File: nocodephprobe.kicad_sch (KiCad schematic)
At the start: 30 parts, among them J1 RF1-01 BNC, J2 10K, Q1 2N7002, U1 LMV358a, U2 ICL7106CPL, U3 MCP1501T-10E/CHY, U4 VI-302-DP-RC-S

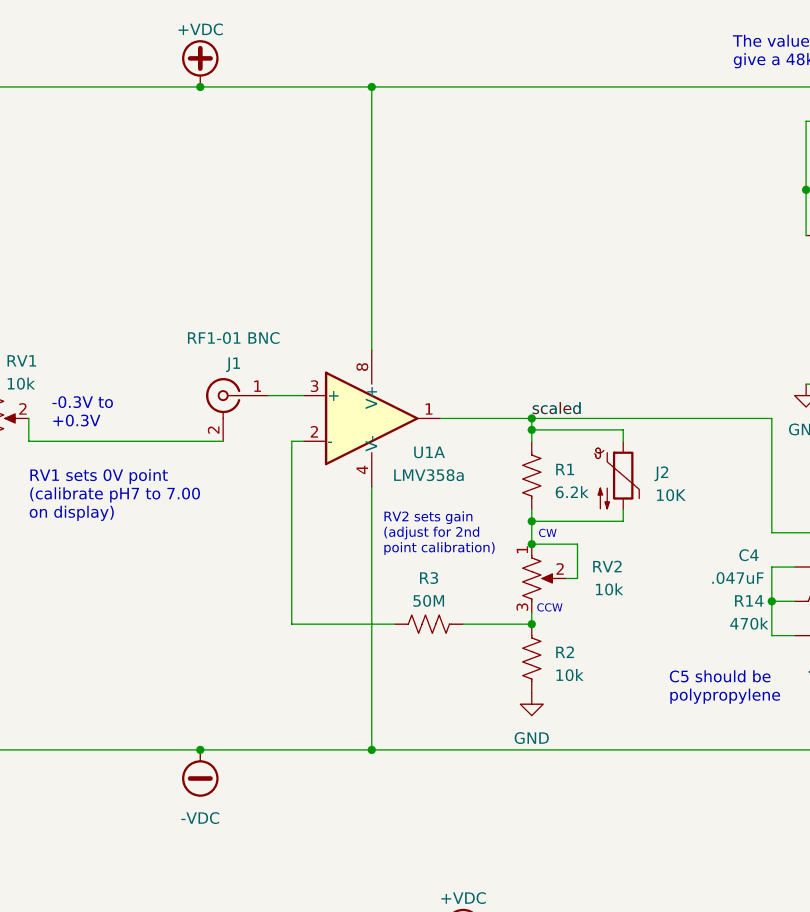
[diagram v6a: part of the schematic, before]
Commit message: schematic: add decoupling caps to op-amp
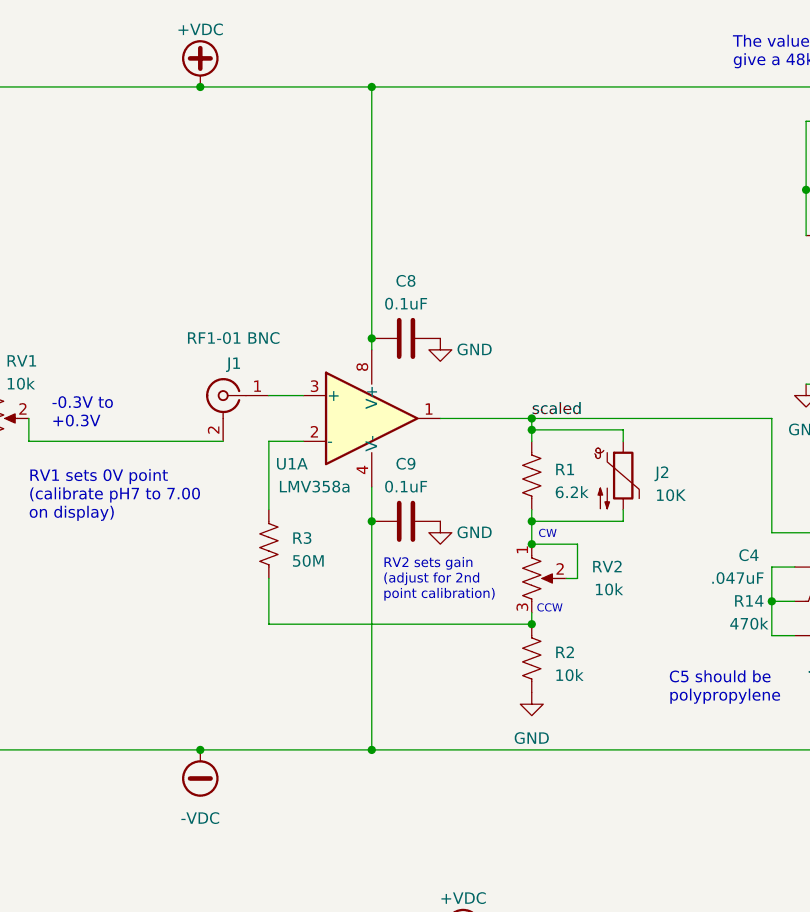
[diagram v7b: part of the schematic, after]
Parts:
- added C8, C9: 0.1uF, Capacitor_SMD:C_0805_2012Metric_Pad1.18x1.45mm_HandSolder, symbol Device:C
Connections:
- net +VDC: now also C8.1
- net -VDC: now also C9.1
- net GND: now also C8.2, C9.2
- net at U1.2 (-): now also R3.1; no longer R3.2
- net at R2.2, RV2.3: now also R3.2; no longer R3.1
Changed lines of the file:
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@@
   (junction (at 68.58 142.24) (diameter 0) (color 0 0 0 0)
   )
+  (junction (at 124.46 54.61) (diameter 0) (color 0 0 0 0)
+  )
   (junction (at 275.59 90.17) (diameter 0) (color 0 0 0 0)
   )
@@
   )
   (junction (at 71.12 74.93) (diameter 0) (color 0 0 0 0)
+  )
+  (junction (at 124.46 74.93) (diameter 0) (color 0 0 0 0)
   )
   (junction (at 275.59 85.09) (diameter 0) (color 0 0 0 0)
@@
     (stroke (width 0) (type default))
   )
+  (wire (pts (xy 113.03 86.36) (xy 142.24 86.36))
+    (stroke (width 0) (type default))
+  )
   (wire (pts (xy 74.93 53.34) (xy 74.93 59.69))
     (stroke (width 0) (type default))
@@
     (stroke (width 0) (type default))
   )
-  (wire (pts (xy 115.57 86.36) (xy 127 86.36))
-    (stroke (width 0) (type default))
-  )
   (wire (pts (xy 82.55 53.34) (xy 74.93 53.34))
     (stroke (width 0) (type default))
@@
     (stroke (width 0) (type default))
   )
+  (wire (pts (xy 124.46 54.61) (xy 124.46 55.88))
+    (stroke (width 0) (type default))
+  )
   (wire (pts (xy 232.41 67.31) (xy 240.03 67.31))
     (stroke (width 0) (type default))
@@
     (stroke (width 0) (type default))
   )
-  (wire (pts (xy 134.62 86.36) (xy 142.24 86.36))
-    (stroke (width 0) (type default))
-  )
   (wire (pts (xy 152.4 64.77) (xy 152.4 66.04))
     (stroke (width 0) (type default))
@@
     (stroke (width 0) (type default))
   )
+  (wire (pts (xy 113.03 73.66) (xy 113.03 66.04))
+    (stroke (width 0) (type default))
+  )
   (wire (pts (xy 232.41 50.8) (xy 217.17 50.8))
     (stroke (width 0) (type default))
@@
     (stroke (width 0) (type default))
   )
-  (wire (pts (xy 124.46 71.12) (xy 124.46 100.33))
-    (stroke (width 0) (type default))
-  )
   (wire (pts (xy 217.17 76.2) (xy 227.33 76.2))
     (stroke (width 0) (type default))
@@
     (stroke (width 0) (type default))
   )
-  (wire (pts (xy 124.46 26.67) (xy 124.46 55.88))
+  (wire (pts (xy 124.46 26.67) (xy 124.46 54.61))
     (stroke (width 0) (type default))
   )
@@
     (stroke (width 0) (type default))
   )
-  (wire (pts (xy 115.57 86.36) (xy 115.57 66.04))
+  (wire (pts (xy 113.03 86.36) (xy 113.03 81.28))
     (stroke (width 0) (type default))
   )
@@
     (stroke (width 0) (type default))
   )
-  (wire (pts (xy 115.57 66.04) (xy 116.84 66.04))
+  (wire (pts (xy 113.03 66.04) (xy 116.84 66.04))
     (stroke (width 0) (type default))
   )
@@
     (stroke (width 0) (type default))
   )
+  (wire (pts (xy 124.46 71.12) (xy 124.46 74.93))
+    (stroke (width 0) (type default))
+  )
   (wire (pts (xy 186.69 86.36) (xy 186.69 87.63))
     (stroke (width 0) (type default))
@@
   )
   (wire (pts (xy 168.91 80.01) (xy 171.45 80.01))
+    (stroke (width 0) (type default))
+  )
+  (wire (pts (xy 124.46 74.93) (xy 124.46 100.33))
     (stroke (width 0) (type default))
   )
@@
     (effects (font (size 1.27 1.27)) (justify left bottom))
   )
-  (text "RV2 sets gain\n(adjust for 2nd\npoint calibration)" (at 125.73 78.74 0)
+  (text "RV2 sets gain\n(adjust for 2nd\npoint calibration)" (at 125.73 83.82 0)
     (effects (font (size 1.0668 1.0668)) (justify left bottom))
   )
@@
     )
   )
+  (symbol (lib_id "Device:R_US") (at 113.03 77.47 0) (unit 1)
+    (in_bom yes) (on_board yes) (dnp no) (fields_autoplaced)
+    (property "Reference" "R3" (at 115.57 76.835 0)
+      (effects (font (size 1.27 1.27)) (justify left))
+    )
+    (property "Value" "50M" (at 115.57 79.375 0)
+      (effects (font (size 1.27 1.27)) (justify left))
+    )
+    (property "Footprint" "Resistor_SMD:R_0805_2012Metric_Pad1.20x1.40mm_HandSolder" (at 114.046 77.724 90)
+      (effects (font (size 1.27 1.27)) hide)
+    )
+    (property "Datasheet" "~" (at 113.03 77.47 0)
+      (effects (font (size 1.27 1.27)) hide)
+    )
+    (pin "1")
+    (pin "2")
+    (instances
+      (project "nocodephprobe"
+        (path "/2036f74b-8ede-4e4d-84df-8cc119de9ab1"
+          (reference "R3") (unit 1)
+        )
+      )
+    )
+  )
+  (symbol (lib_id "power:GND") (at 132.08 54.61 0) (unit 1)
+    (in_bom yes) (on_board yes) (dnp no)
+    (property "Reference" "#PWR012" (at 132.08 60.96 0)
+      (effects (font (size 1.27 1.27)) hide)
+    )
+    (property "Value" "GND" (at 135.89 55.88 0)
+      (effects (font (size 1.27 1.27)))
+    )
+    (property "Footprint" "" (at 132.08 54.61 0)
+      (effects (font (size 1.27 1.27)) hide)
+    )
+    (property "Datasheet" "" (at 132.08 54.61 0)
+      (effects (font (size 1.27 1.27)) hide)
+    )
+    (pin "1")
+    (instances
+      (project "nocodephprobe"
+        (path "/2036f74b-8ede-4e4d-84df-8cc119de9ab1"
+          (reference "#PWR012") (unit 1)
+        )
+      )
+    )
+  )
   (symbol (lib_id "Device:C") (at 205.74 100.33 90) (unit 1)
     (in_bom yes) (on_board yes) (dnp no)
@@
   (symbol (lib_id "Amplifier_Operational:LMV358") (at 124.46 63.5 0) (unit 1)
     (in_bom yes) (on_board yes) (dnp no)
-    (property "Reference" "U1" (at 130.81 67.31 0)
-      (effects (font (size 1.27 1.27)))
-    )
-    (property "Value" "LMV358a" (at 130.81 69.85 0)
+    (property "Reference" "U1" (at 115.57 68.58 0)
+      (effects (font (size 1.27 1.27)))
+    )
+    (property "Value" "LMV358a" (at 118.11 71.12 0)
       (effects (font (size 1.27 1.27)))
     )
@@
     )
   )
-  (symbol (lib_id "Device:R_US") (at 130.81 86.36 270) (unit 1)
-    (in_bom yes) (on_board yes) (dnp no) (fields_autoplaced)
-    (property "Reference" "R3" (at 130.81 81.28 90)
-      (effects (font (size 1.27 1.27)))
-    )
-    (property "Value" "50M" (at 130.81 83.82 90)
-      (effects (font (size 1.27 1.27)))
-    )
-    (property "Footprint" "Resistor_SMD:R_0805_2012Metric_Pad1.20x1.40mm_HandSolder" (at 130.556 87.376 90)
-      (effects (font (size 1.27 1.27)) hide)
-    )
-    (property "Datasheet" "~" (at 130.81 86.36 0)
-      (effects (font (size 1.27 1.27)) hide)
-    )
-    (pin "1")
-    (pin "2")
-    (instances
-      (project "nocodephprobe"
-        (path "/2036f74b-8ede-4e4d-84df-8cc119de9ab1"
-          (reference "R3") (unit 1)
+  (symbol (lib_id "Device:C") (at 128.27 54.61 90) (unit 1)
+    (in_bom yes) (on_board yes) (dnp no) (fields_autoplaced)
+    (property "Reference" "C8" (at 128.27 48.26 90)
+      (effects (font (size 1.27 1.27)))
+    )
+    (property "Value" "0.1uF" (at 128.27 50.8 90)
+      (effects (font (size 1.27 1.27)))
+    )
+    (property "Footprint" "Capacitor_SMD:C_0805_2012Metric_Pad1.18x1.45mm_HandSolder" (at 132.08 53.6448 0)
+      (effects (font (size 1.27 1.27)) hide)
+    )
+    (property "Datasheet" "~" (at 128.27 54.61 0)
+      (effects (font (size 1.27 1.27)) hide)
+    )
+    (pin "1")
+    (pin "2")
+    (instances
+      (project "nocodephprobe"
+        (path "/2036f74b-8ede-4e4d-84df-8cc119de9ab1"
+          (reference "C8") (unit 1)
+        )
+      )
+    )
+  )
+  (symbol (lib_id "Device:C") (at 128.27 74.93 90) (unit 1)
+    (in_bom yes) (on_board yes) (dnp no) (fields_autoplaced)
+    (property "Reference" "C9" (at 128.27 68.58 90)
+      (effects (font (size 1.27 1.27)))
+    )
+    (property "Value" "0.1uF" (at 128.27 71.12 90)
+      (effects (font (size 1.27 1.27)))
+    )
+    (property "Footprint" "Capacitor_SMD:C_0805_2012Metric_Pad1.18x1.45mm_HandSolder" (at 132.08 73.9648 0)
+      (effects (font (size 1.27 1.27)) hide)
+    )
+    (property "Datasheet" "~" (at 128.27 74.93 0)
+      (effects (font (size 1.27 1.27)) hide)
+    )
+    (pin "1")
+    (pin "2")
+    (instances
+      (project "nocodephprobe"
+        (path "/2036f74b-8ede-4e4d-84df-8cc119de9ab1"
+          (reference "C9") (unit 1)
         )
       )
@@
         )
       )
+    )
+  )
+  (symbol (lib_id "power:GND") (at 132.08 74.93 0) (unit 1)
+    (in_bom yes) (on_board yes) (dnp no)
+    (property "Reference" "#PWR013" (at 132.08 81.28 0)
+      (effects (font (size 1.27 1.27)) hide)
+    )
+    (property "Value" "GND" (at 135.89 76.2 0)
+      (effects (font (size 1.27 1.27)))
+    )
+    (property "Footprint" "" (at 132.08 74.93 0)
+      (effects (font (size 1.27 1.27)) hide)
+    )
+    (property "Datasheet" "" (at 132.08 74.93 0)
+      (effects (font (size 1.27 1.27)) hide)
+    )
+    (pin "1")
+    (instances
+      (project "nocodephprobe"
+        (path "/2036f74b-8ede-4e4d-84df-8cc119de9ab1"
+          (reference "#PWR013") (unit 1)
+        )
+      )

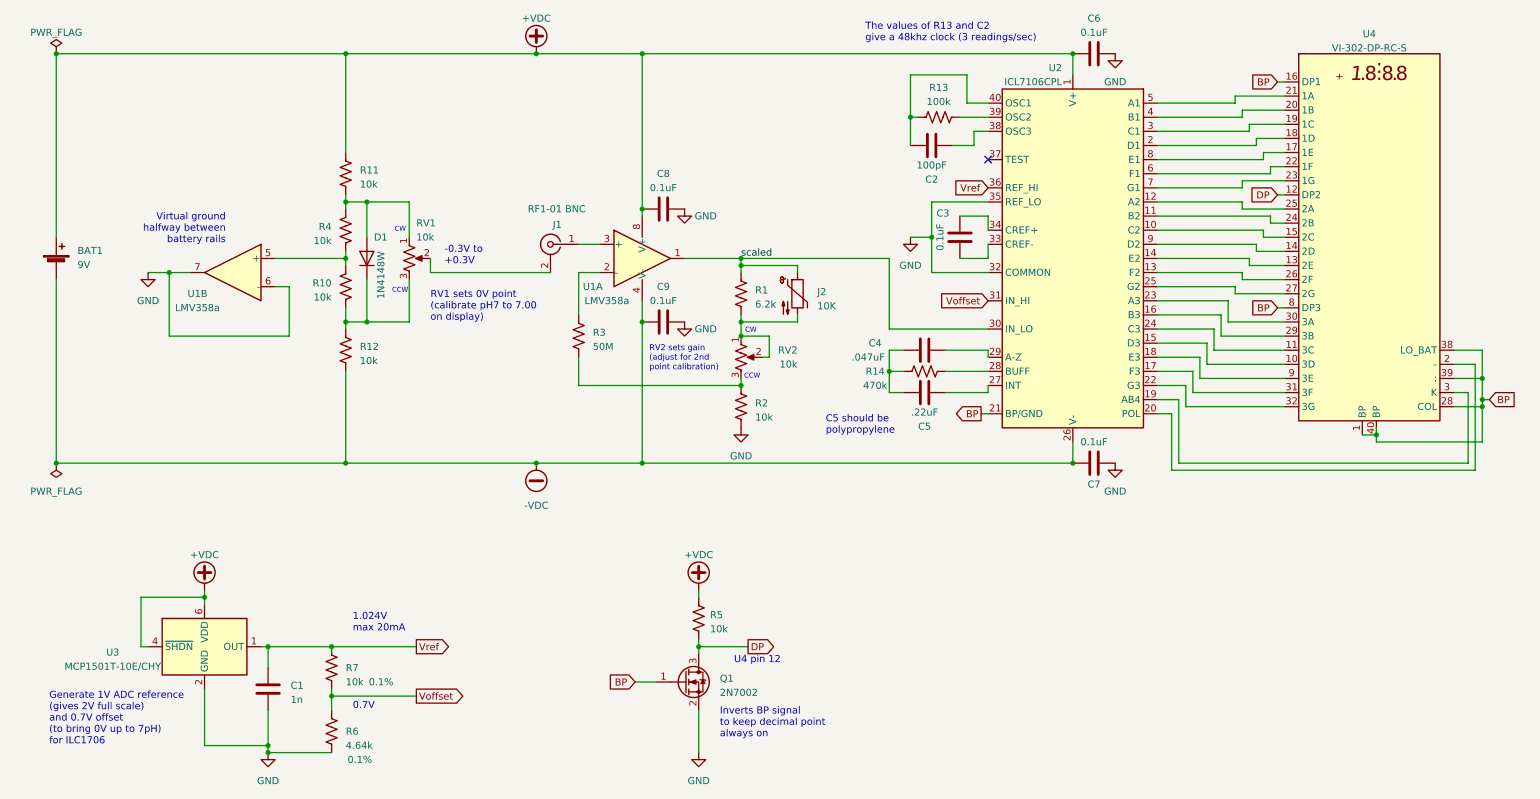
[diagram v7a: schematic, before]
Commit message: Fix op-amp power supply
Add an 7805 linear regulator to keep voltage within max supply, and add
decoupling caps.
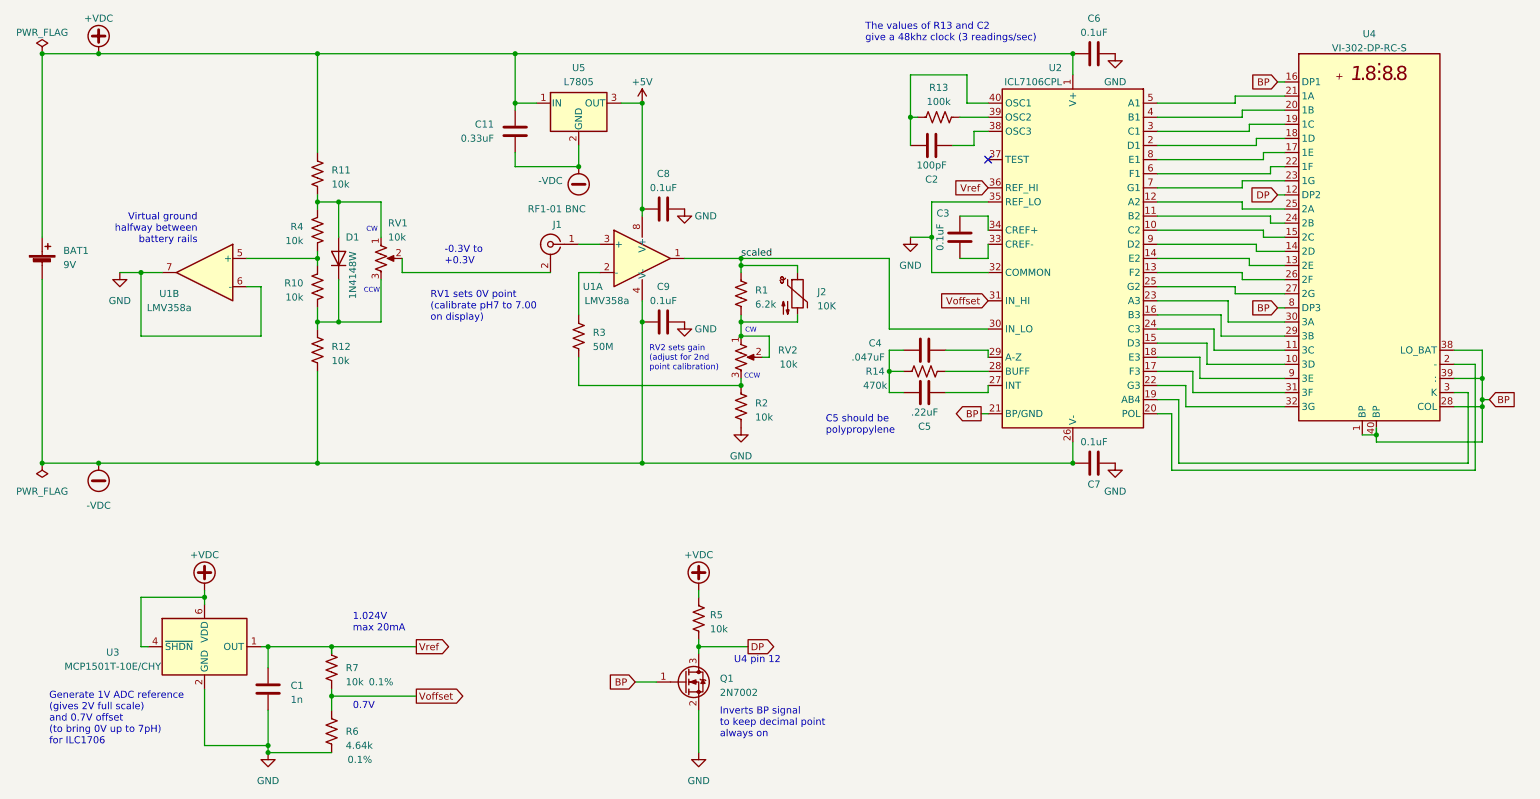
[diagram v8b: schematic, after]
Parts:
- added C11: 0.33uF, Capacitor_SMD:C_0805_2012Metric_Pad1.18x1.45mm_HandSolder, symbol Device:C
- added U5: L7805, Package_TO_SOT_SMD:TO-252-3_TabPin2, symbol Regulator_Linear:L7805
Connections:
- net +VDC: now also C11.2, U5.1 (IN); no longer C8.1, U1.8 (V+)
- net -VDC: now also C11.1, U5.2 (GND)
- new net +5V: C8.1, U1.8 (V+), U5.3 (OUT)
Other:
- moved on the sheet: BAT1, D1, R10, R11, R12, R4, RV1, U1B
